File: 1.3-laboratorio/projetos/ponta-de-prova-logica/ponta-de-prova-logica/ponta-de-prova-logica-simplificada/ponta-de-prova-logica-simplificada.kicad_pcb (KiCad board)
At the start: 2 copper layers, 17 parts, among them J1 TEST PROBE, U1 LM319

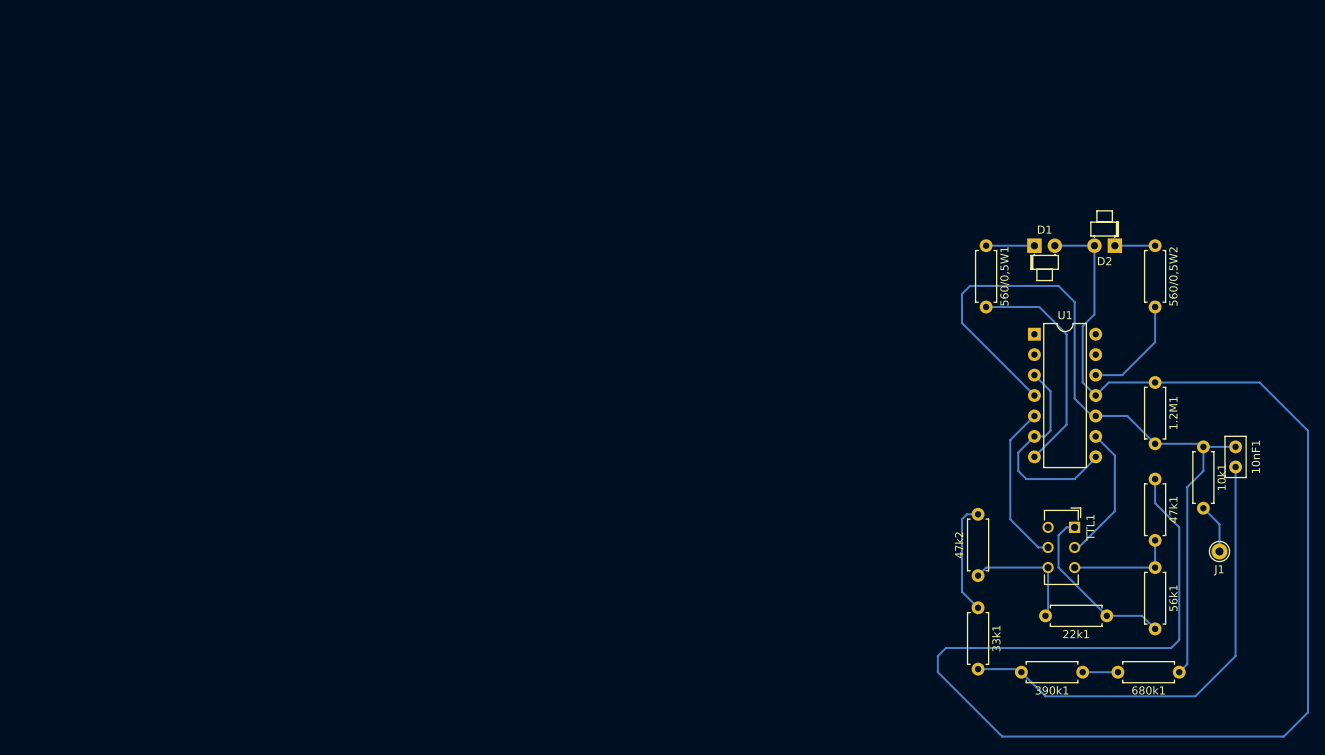
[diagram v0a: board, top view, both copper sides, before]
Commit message: Esquema da ponta de prova lógica atualizado
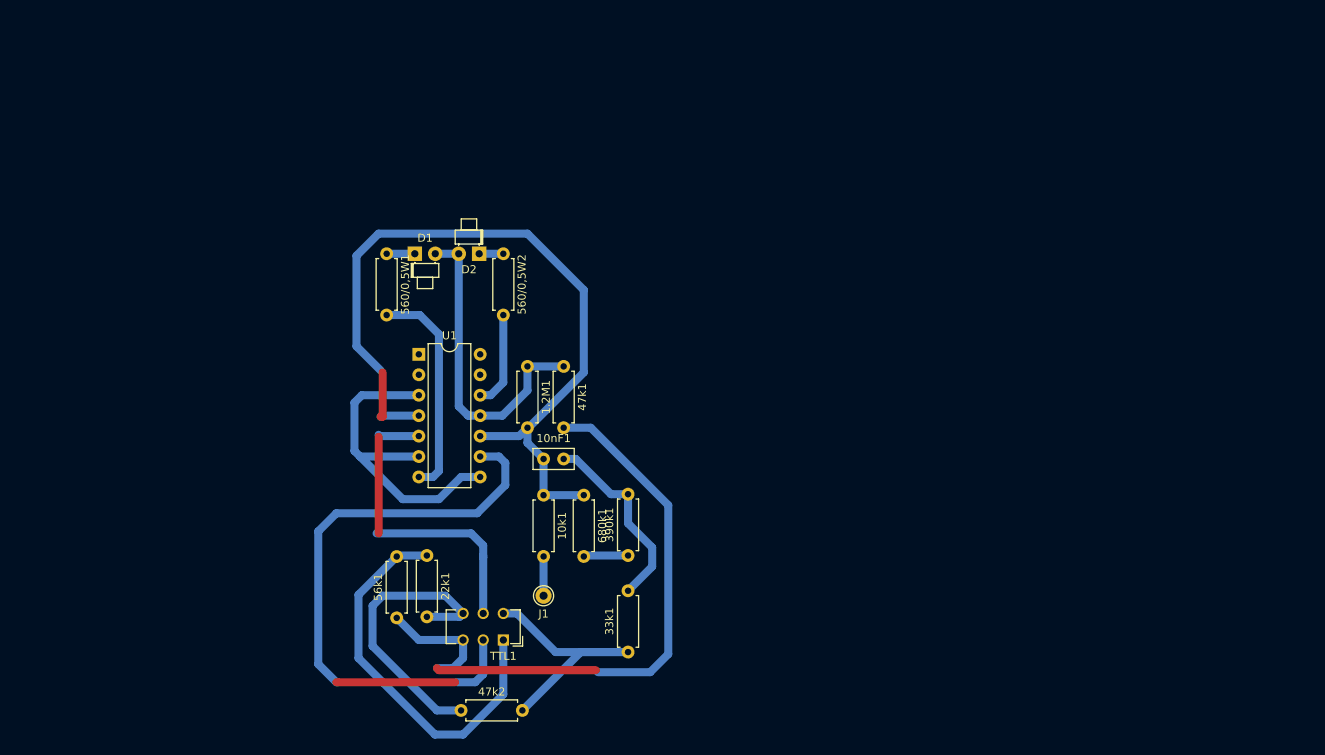
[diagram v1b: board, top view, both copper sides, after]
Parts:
- moved 56k1 94.5 mm to (131.8, 129.2), turned to 90 degrees
- moved 10nF1 86.0 mm to (150.0, 109.5), turned to 0 degrees
- moved 22k1 84.8 mm to (135.5, 121.5), turned to 270 degrees
- moved J1 84.2 mm to (150.0, 126.5)
- moved 10k1 82.2 mm to (150.0, 114.0)
- moved 560/0,5W2 81.0 mm to (145.0, 84.0)
- moved D2 79.0 mm to (142.0, 84.0)
- moved 1.2M1 78.0 mm to (148.0, 98.0)
- moved 680k1 77.2 mm to (155.0, 114.0), turned to 270 degrees
- moved D1 77.0 mm to (134.0, 84.0)
- moved U1 76.5 mm to (134.5, 96.5)
- moved 47k1 74.8 mm to (152.5, 98.0)
- moved 560/0,5W1 74.5 mm to (130.5, 84.0)
- moved TTL1 72.4 mm to (145.0, 132.0), turned to 180 degrees
- moved 47k2 66.4 mm to (139.8, 140.8), turned to 0 degrees
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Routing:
- net +5V: track 194.0 -> 39.7 mm
- net (no net): track 0.00 -> 52.4 mm
- net 77%: track 13.4 -> 60.6 mm
- net Net-(TTL1-Pad2): track 17.1 -> 59.7 mm
- net Net-(10nF1-Pad2): track 59.0 -> 24.3 mm
- net Net-(22k1-Pad1): track 21.6 -> 49.1 mm
- net 39%: track 15.2 -> 36.7 mm
- net Net-(33k1-Pad1): track 14.1 -> 33.6 mm
- net GND: track 26.4 -> 40.9 mm
- net Net-(TTL1-Pad5): track 20.2 -> 27.6 mm
- net Net-(560/0,5W1-Pad1): track 6.00 -> 3.50 mm
- net Net-(1.2M1-Pad2): track 95.3 -> 93.2 mm
- net Net-(560/0,5W2-Pad1): track 5.00 -> 3.00 mm
- net Net-(560/0,5W1-Pad2): track 28.8 -> 27.3 mm
- net Net-(560/0,5W2-Pad2): track 13.4 -> 11.9 mm
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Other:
- net class Default: clearance 0.2 -> 0.5; trace_width 0.25 -> 1
- rule trace_clearance: 0.2 -> 0.5

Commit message: Atualização dos arquivos para nova versão do KiCad.
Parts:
- removed 1.2M1, 10k1, 22k1, 33k1, 390k1, 47k1, 47k2, 560/0,5W1, 560/0,5W2, 56k1, 680k1: R, Resistors_THT:R_Axial_DIN0207_L6.3mm_D2.5mm_P7.62mm_Horizontal
- removed 10nF1: C, Capacitors_THT:C_Disc_D5.0mm_W2.5mm_P2.50mm
- added C1: 10nF, Capacitors_THT:C_Disc_D5.0mm_W2.5mm_P2.50mm, F.Cu at (94.0, 111.5)
- added J2: Conn_01x02, TerminalBlocks_Phoenix:TerminalBlock_Phoenix_MKDS1.5-2pol, F.Cu at (92.0, 76.8)
- added R1: 47k, Resistors_THT:R_Axial_DIN0207_L6.3mm_D2.5mm_P7.62mm_Horizontal, F.Cu at (143.8, 82.5)
- added R10: 680k, Resistors_THT:R_Axial_DIN0207_L6.3mm_D2.5mm_P7.62mm_Horizontal, F.Cu at (109.8, 110.2)
- added R11: 390k, Resistors_THT:R_Axial_DIN0207_L6.3mm_D2.5mm_P7.62mm_Horizontal, F.Cu at (117.8, 104.5)
- added R2: 1.2M, Resistors_THT:R_Axial_DIN0207_L6.3mm_D2.5mm_P7.62mm_Horizontal, F.Cu at (85.2, 88.2)
- added R3: 560/0.5W, Resistors_THT:R_Axial_DIN0207_L6.3mm_D2.5mm_P7.62mm_Horizontal, F.Cu at (167.0, 91.5)
- added R4: 56k, Resistors_THT:R_Axial_DIN0207_L6.3mm_D2.5mm_P7.62mm_Horizontal, F.Cu at (122.5, 78.2)
- added R5: 22k, Resistors_THT:R_Axial_DIN0207_L6.3mm_D2.5mm_P7.62mm_Horizontal, F.Cu at (124.2, 90.5)
- added R6: 10k, Resistors_THT:R_Axial_DIN0207_L6.3mm_D2.5mm_P7.62mm_Horizontal, F.Cu at (93.5, 101.2)
- added R7: 560/0.5W, Resistors_THT:R_Axial_DIN0207_L6.3mm_D2.5mm_P7.62mm_Horizontal, F.Cu at (134.5, 74.0)
- added R8: 47k, Resistors_THT:R_Axial_DIN0207_L6.3mm_D2.5mm_P7.62mm_Horizontal, F.Cu at (132.2, 108.8)
- added R9: 33k, Resistors_THT:R_Axial_DIN0207_L6.3mm_D2.5mm_P7.62mm_Horizontal, F.Cu at (120.2, 69.2)
- TTL1: value CMOS -> SW_DPDT_x2
- moved TTL1 76.3 mm to (128.8, 57.5), turned to 0 degrees
- moved J1 52.3 mm to (104.2, 101.2)
- moved D2 33.9 mm to (118.2, 59.8), turned to 0 degrees
- moved D1 33.6 mm to (107.2, 63.8)
- moved U1 29.7 mm to (110.5, 79.0)
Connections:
- TTL1 pad 3: 77% -> Net-(R1-Pad2)
- TTL1 pad 6: 39% -> Net-(R5-Pad2)
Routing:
- net Net-(C1-Pad1): track 93.2 -> 0.00 mm
- net 77%: track 60.6 -> 0.00 mm
- net Net-(TTL1-Pad2): track 59.7 -> 0.00 mm
- net (no net): track 52.4 -> 0.00 mm
- net Net-(R4-Pad2): track 49.1 -> 0.00 mm
- net GND: track 40.9 -> 0.00 mm
- net +5V: track 39.7 -> 0.00 mm
- net 39%: track 36.7 -> 0.00 mm
- net Net-(R8-Pad2): track 33.6 -> 0.00 mm
- net Net-(TTL1-Pad5): track 27.6 -> 0.00 mm
- net Net-(R3-Pad2): track 27.3 -> 0.00 mm
- net Net-(10nF1-Pad2): track 24.3 -> 0.00 mm
- net Net-(R7-Pad2): track 11.9 -> 0.00 mm
- net Net-(390k1-Pad1): track 5.55 -> 0.00 mm
- net Net-(J1-Pad1): track 4.88 -> 0.00 mm
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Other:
- net class Default: clearance 0.5 -> 0.2; trace_width 1 -> 0.25; via_dia 0.6 -> 0.8
- rule trace_clearance: 0.5 -> 0.2
